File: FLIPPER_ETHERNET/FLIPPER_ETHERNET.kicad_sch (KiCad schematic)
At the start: 31 parts, among them IC1 MC74ACT125DTR2G, J1 RJ45_Hanrun_HR911105A_Horizon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, J2 Screw_Terminal_01x06, SW1 SW_Push, T1 HX1188NLT, U1 ENC28J60x-ML, Y1 25MHz

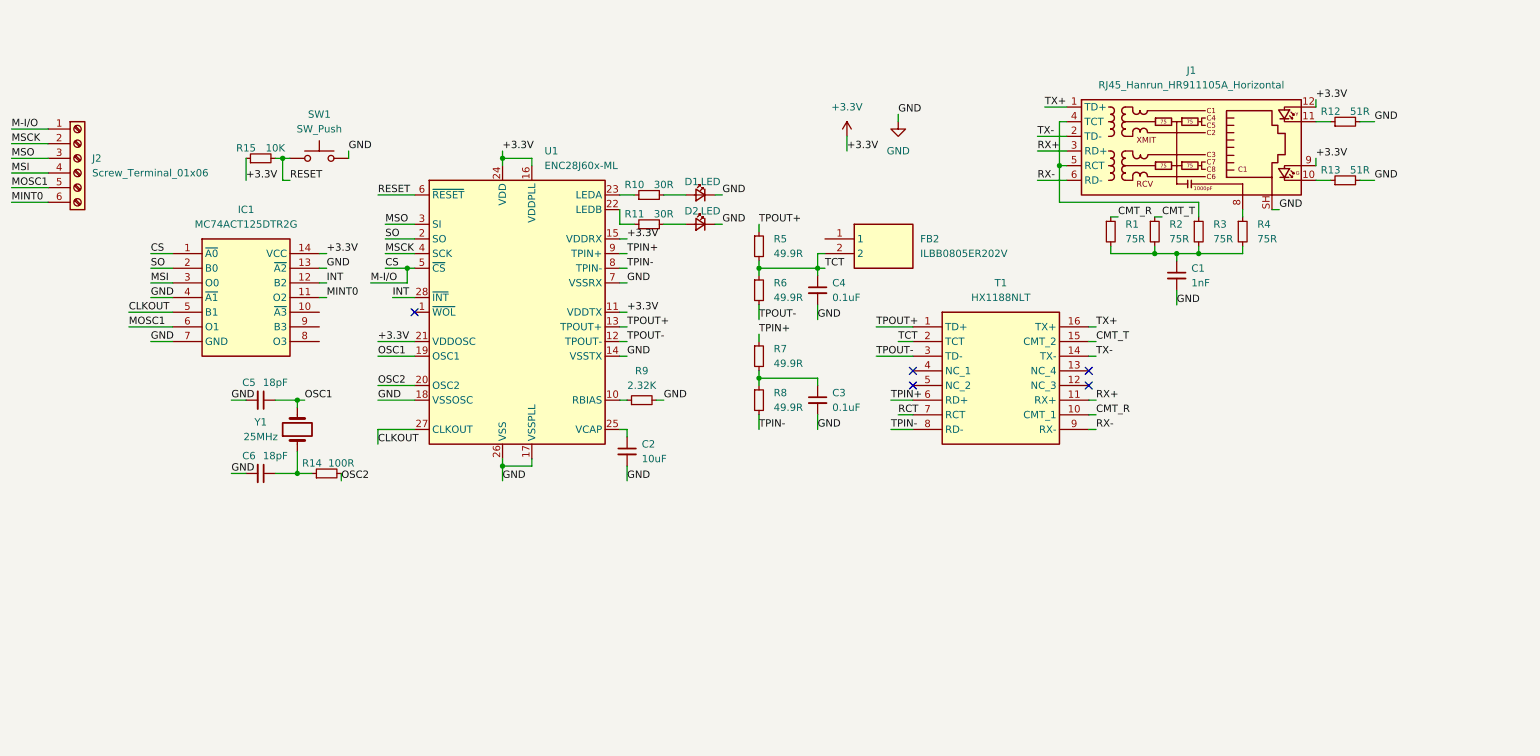
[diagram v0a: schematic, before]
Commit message: feat: component reduction in the schematic of flipper ethernet and pcb first draft
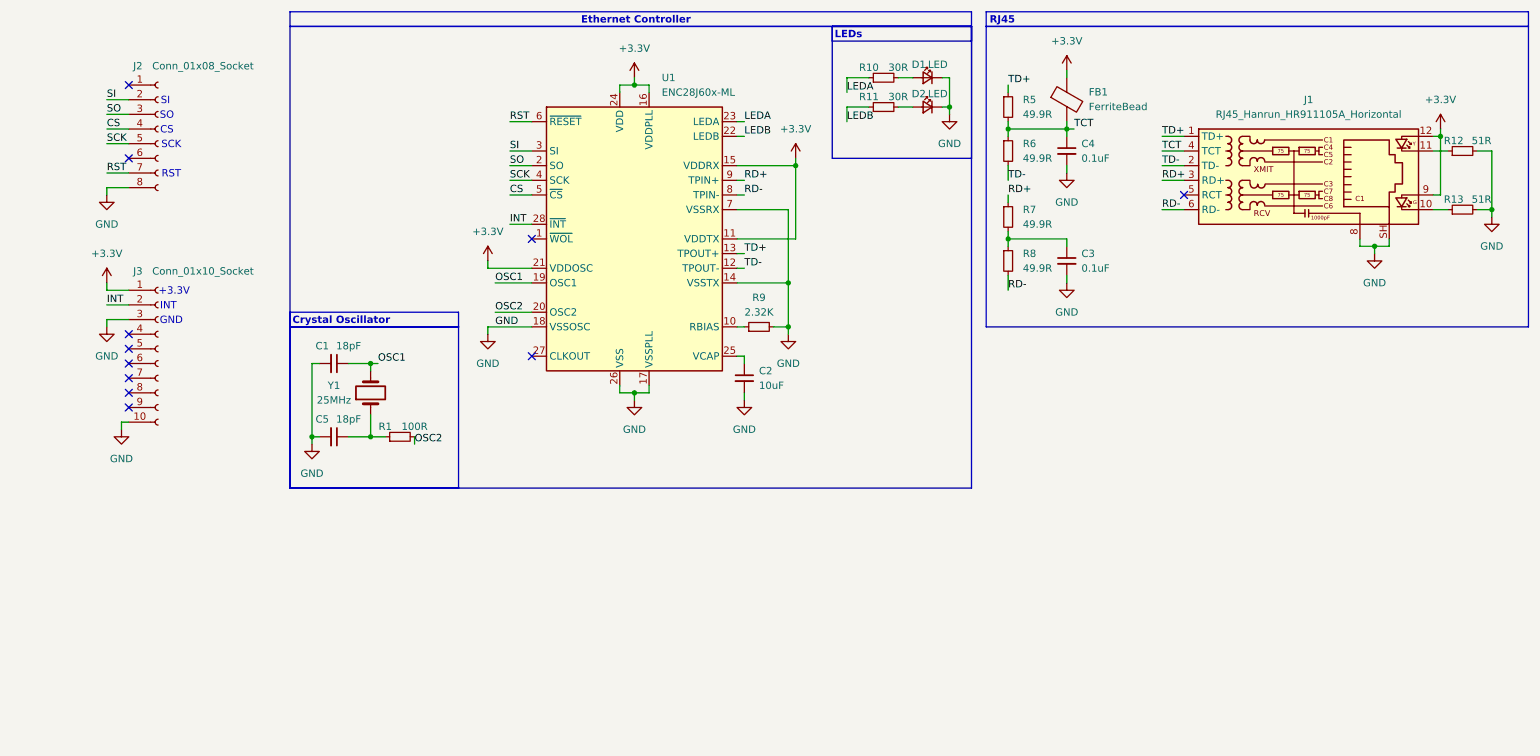
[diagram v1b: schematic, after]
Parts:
- removed C6: 18pF, Capacitor_SMD:C_0603_1608Metric, symbol Device:C_Small
- removed FB2: ILBB0805ER202V, Inductor_SMD:L_Walsin_WLFM201209x, symbol ILBB0805ER202V:ILBB0805ER202V
- removed IC1: MC74ACT125DTR2G, FLIPPER_ETHERNET:MC74ACT125DTR2G, symbol MC74ACT125DTR2G:MC74ACT125DTR2G
- removed J2: Screw_Terminal_01x06, TerminalBlock:TerminalBlock_Xinya_XY308-2.54-6P_1x06_P2.54mm_Horizontal, symbol Connector:Screw_Terminal_01x06
- removed R14: 100R, Resistor_SMD:R_0603_1608Metric, symbol Device:R_Small
- removed R15: 10K, Resistor_SMD:R_0603_1608Metric, symbol Device:R_Small
- removed R2, R3, R4: 75R, Resistor_SMD:R_0603_1608Metric, symbol Device:R_Small
- removed SW1: SW_Push, Button_Switch_THT:SW_Tactile_Straight_KSA0Axx1LFTR, symbol Switch:SW_Push
- removed T1: HX1188NLT, Transformer_SMD:Transformer_Pulse_H1100NL, symbol HX1188NLT:HX1188NLT
- added FB1: FerriteBead, Inductor_SMD:L_Walsin_WLFM201209x, symbol Device:FerriteBead
- added J2: Conn_01x08_Socket, Connector_PinHeader_2.54mm:PinHeader_1x08_P2.54mm_Vertical, symbol Connector:Conn_01x08_Socket
- added J3: Conn_01x10_Socket, Connector_PinHeader_2.54mm:PinHeader_1x10_P2.54mm_Vertical, symbol Connector:Conn_01x10_Socket
- C1: value 1nF -> 18pF
- R1: value 75R -> 100R
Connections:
- net CMT_R is gone; now on an unnamed net: R1.1
- net TPIN+ is gone; now on net RD+: R7.1, U1.9 (TPIN+)
- net TPIN- is gone; now on net RD-: R8.2, U1.8 (TPIN-)
- net TX+ is gone; now on net TD+: J1.1 (TD+)
- net TX- is gone; now on net TD-: J1.2 (TD-)
- net +3.3V: now also FB1.1, J3.1 (Pin_1)
- net CS: now also J2.4 (Pin_4)
- net GND: now also J1.8, J2.8 (Pin_8), J3.10 (Pin_10), J3.3 (Pin_3)
- net INT: now also J3.2 (Pin_2)
- net OSC1: now also C1.1; no longer C5.1
- net OSC2: now also R1.2
- net SO: now also J2.3 (Pin_3)
- net TCT: now also J1.4 (TCT), FB1.2
- net at Y1.1: now also C5.1
- net at J1.5 (RCT): no longer J1.4 (TCT)
- net LEDB: now reaches R11.1, U1.22 (LEDB)
- net LEDA: now reaches R10.1, U1.23 (LEDA)
- net CLKOUT: no longer names the net of U1.27 (CLKOUT)
- net MSCK renamed SCK
- net SCK: now also J2.5 (Pin_5)
- net MSO renamed SI
- net SI: now also J2.2 (Pin_2)
- net RESET renamed RST
- net RST: now also J2.7 (Pin_7)
- net RX+ renamed RD+
- net RX- renamed RD-
- net TPOUT+ renamed TD+
- net TPOUT- renamed TD-
- no-connect marks 5 -> 11
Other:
- note added: "+3.3V"
- note added: "CS"
- note added: "Crystal Oscillator"
- note added: "Ethernet Controller"
- note added: "GND"
- note added: "INT"
- note added: "LEDs"
- note added: "RJ45"
- note added: "RST"
- note added: "SCK"
- note added: "SI"
- note added: "SO"
- moved on the sheet: C2, C3, C4, D1, D2, J1, R10, R11, R12, R13, R5, R6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

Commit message: feat: second draft of flipper ethernet pcb
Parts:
- added R2: 10K, Resistor_SMD:R_0603_1608Metric, symbol Device:R_Small
- added SW1: SW_Push, Button_Switch_THT:SW_Tactile_Straight_KSA0Axx1LFTR, symbol Switch:SW_Push
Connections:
- net +3.3V: now also R2.1
- net GND: now also SW1.2
- net RST: no longer names the net of J2.7 (Pin_7)
- net RST: no longer U1.6 (~{RESET})
- new net RESET: R2.2, SW1.1, U1.6 (~{RESET})
- no-connect marks 11 -> 12
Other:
- note removed: "RST"

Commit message: feat: pcb corrected for possible first flipper ethernet prototype
all 3d models added
all labels added and reorganized
button changed for smd metal button
components reorganized
leds deleted
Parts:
- removed D1, D2: LED, LED_SMD:LED_0603_1608Metric, symbol Device:LED_Small
- removed R10, R11: 30R, Resistor_SMD:R_0603_1608Metric, symbol Device:R_Small
- SW1: footprint Button_Switch_THT:SW_Tactile_Straight_KSA0Axx1LFTR -> Button_Switch_SMD:SW_SPST_TL3342
- Y1: footprint FLIPPER_ETHERNET:ABLS-25.000MHZ-20-F-T -> Crystal:Crystal_SMD_HC49-SD
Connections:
- net +3.3V: no longer J1.12, J1.9
- net LEDA: now also J1.9
- net LEDB: now also J1.12
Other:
- note removed: "LEDs"

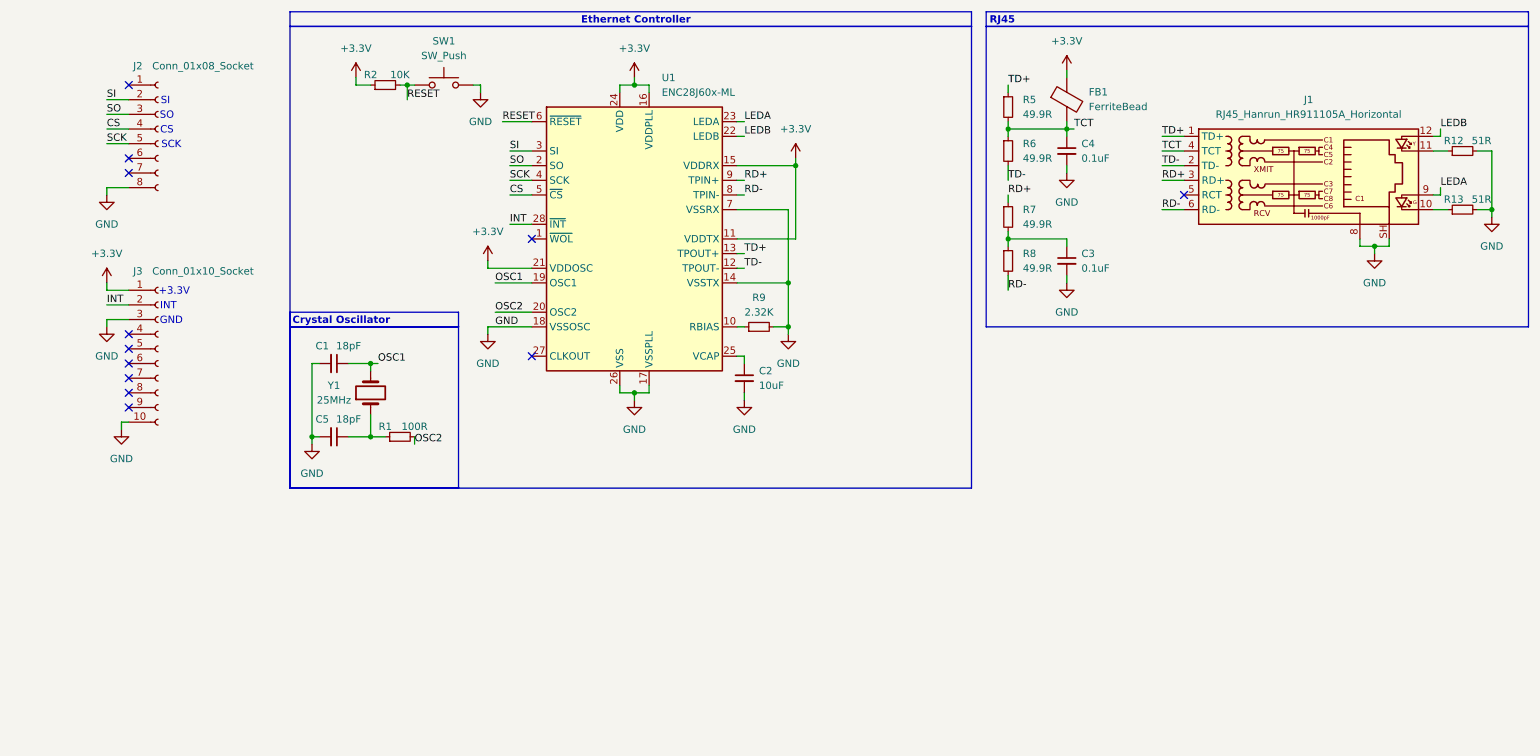
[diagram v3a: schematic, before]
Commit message: feat: bom added
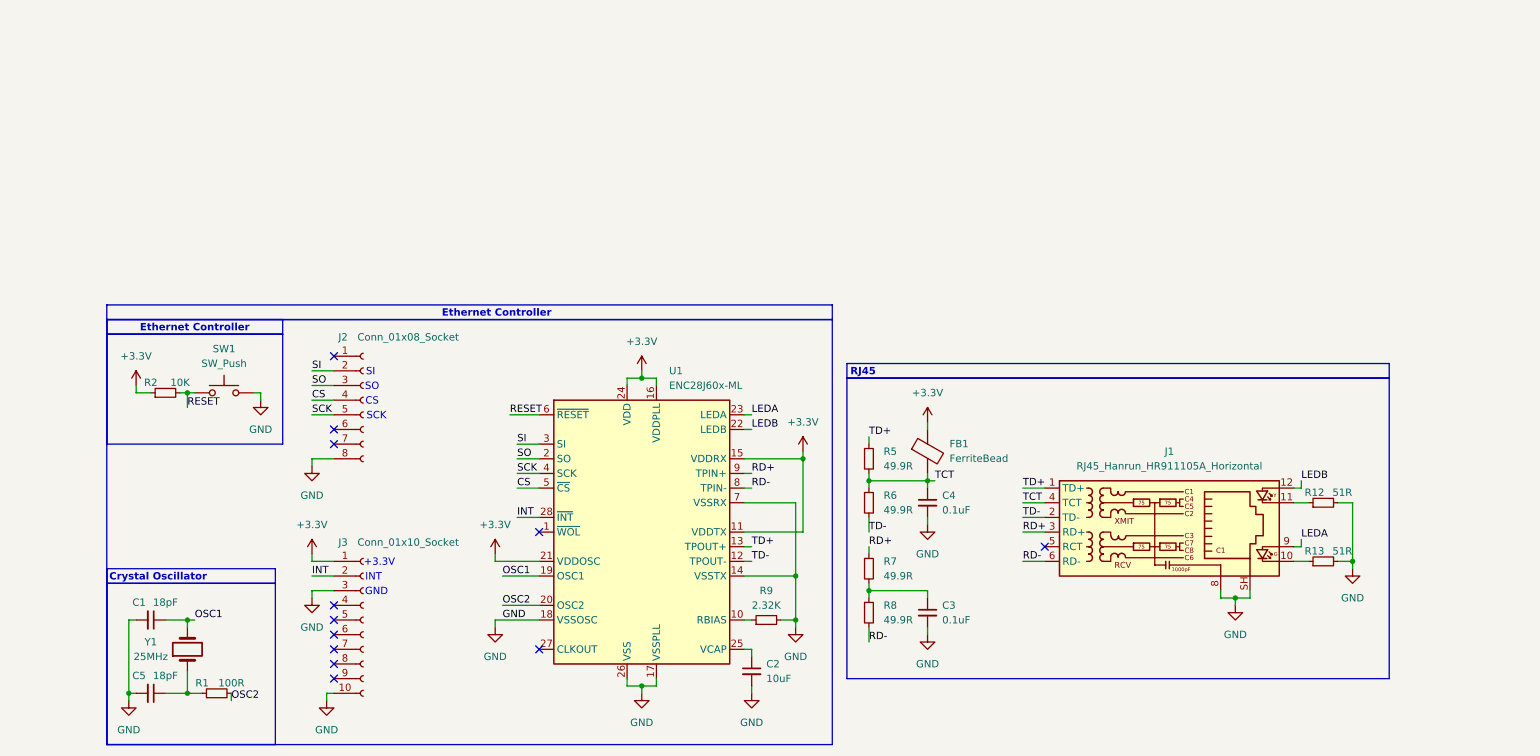
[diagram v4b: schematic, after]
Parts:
- C1, C5: #LSCS (none) -> C3870208; Proveedor (none) -> LCSC; manf# (none) -> 600S180FT250XT
- C2: #LSCS (none) -> C192094; Proveedor (none) -> LCSC; manf# (none) -> GRM188R60J106ME84D
- C3, C4: #LSCS (none) -> C20214933; Proveedor (none) -> LCSC; manf# (none) -> KGF15AR71E104JT
- FB1: #LSCS (none) -> C6639322; Proveedor (none) -> LCSC; manf# (none) -> ILBB0805ER202V
- J1: #LSCS (none) -> C12074; Proveedor (none) -> LCSC; manf# (none) -> HR911105A
- J2, J3: #LSCS (none) -> C7501580; Proveedor (none) -> LCSC; manf# (none) -> PH2.54-01-02PZD
- R1: #LSCS (none) -> C6888379; Proveedor (none) -> LCSC; manf# (none) -> CRT0603-BY-1000ELF
- R12, R13: #LSCS (none) -> C4051836; Proveedor (none) -> LCSC; manf# (none) -> SFR03EZPJ510
- R2: #LSCS (none) -> C4199414; Proveedor (none) -> LCSC; manf# (none) -> CAR0603-10KB2
- R5, R6, R7, R8: #LSCS (none) -> C6976359; Proveedor (none) -> LCSC; manf# (none) -> RMC1/16K49R9FTP
- R9: #LSCS (none) -> C4139945; Proveedor (none) -> LCSC; manf# (none) -> ERJ-PA3F2321V
- SW1: #LSCS (none) -> C2886897; Proveedor (none) -> LCSC; manf# (none) -> TL3342F450QG
- U1: #LSCS (none) -> C57281; Proveedor (none) -> LCSC; manf# (none) -> ENC28J60-I/ML
- Y1: footprint Crystal:Crystal_SMD_HC49-SD -> FLIPPER_ETHERNET:ABLS-25.000MHZ-20-F-T; #LSCS (none) -> C5572271; Proveedor (none) -> LCSC; manf# (none) -> ABLS-25.000MHZ-20-F-T
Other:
- company: (none) -> Electronic Cats
- title: (none) -> FLIPPER ADDON ETHERNET V1.0
- moved on the sheet: C1, C2, C3, C4, C5, FB1, J1, J2, J3, R1, R12, R13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
